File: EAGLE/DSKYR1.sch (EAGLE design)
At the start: 6 parts, among them IC1 74HC595N, IC2 74HC595N, IC3 74HC595N

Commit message: Update guide, finalize gerber files
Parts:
- SV1: device con-lstb:MA05-1 -> con-lsta:FE06-1
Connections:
- removed net N$5: IC1A.SCL, IC2A.SCL, IC3A.SCL, SV1.3
- new net GND: SV1.1
- new net VCC: IC1A.SCL, IC2A.SCL, IC3A.SCL, SV1.4
- net N$1: now also SV1.6; no longer SV1.5
- net N$4: now also SV1.5; no longer SV1.4
- net N$6: now also SV1.2; no longer SV1.1
- net N$8: now also SV1.3; no longer SV1.2
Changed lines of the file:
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@@
 <part name="IC2" library="74xx-eu" library_urn="urn:adsk.eagle:library:85" deviceset="74*595" device="N" package3d_urn="urn:adsk.eagle:package:922/2" technology="HC"/>
 <part name="IC3" library="74xx-eu" library_urn="urn:adsk.eagle:library:85" deviceset="74*595" device="N" package3d_urn="urn:adsk.eagle:package:922/2" technology="HC"/>
-<part name="SV1" library="con-lstb" library_urn="urn:adsk.eagle:library:162" deviceset="MA05-1" device="" package3d_urn="urn:adsk.eagle:package:8332/1"/>
 <part name="D1" library="special" library_urn="urn:adsk.eagle:library:367" deviceset="7SEG-CK" device="" package3d_urn="urn:adsk.eagle:package:26668/2"/>
 <part name="DIS1" library="display-nfd" deviceset="NFD-5641AS-ALT" device=""/>
+<part name="P+1" library="supply1" library_urn="urn:adsk.eagle:library:371" deviceset="VCC" device=""/>
+<part name="SV1" library="con-lsta" library_urn="urn:adsk.eagle:library:161" deviceset="FE06-1" device="" package3d_urn="urn:adsk.eagle:package:8191/1"/>
+<part name="GND1" library="supply1" library_urn="urn:adsk.eagle:library:371" deviceset="GND" device=""/>
 </parts>
 <sheets>
@@
 <attribute name="VALUE" x="88.9" y="15.24" size="1.778" layer="96"/>
 </instance>
-<instance part="SV1" gate="G$1" x="-30.48" y="-35.56" smashed="yes">
-<attribute name="VALUE" x="-31.75" y="-45.72" size="1.778" layer="96"/>
-<attribute name="NAME" x="-31.75" y="-27.178" size="1.778" layer="95"/>
-</instance>
 <instance part="D1" gate="G$1" x="91.44" y="-76.2" smashed="yes">
 <attribute name="NAME" x="86.36" y="-67.945" size="1.778" layer="95"/>
@@
 <attribute name="NAME" x="30.353" y="-81.28" size="1.778" layer="95" rot="R90"/>
 <attribute name="VALUE" x="62.738" y="-81.28" size="1.778" layer="96" rot="R90"/>
+</instance>
+<instance part="P+1" gate="VCC" x="-30.48" y="35.56" smashed="yes" rot="R90">
+<attribute name="VALUE" x="-27.94" y="33.02" size="1.778" layer="96" rot="R180"/>
+</instance>
+<instance part="SV1" gate="G$1" x="-30.48" y="-38.1" smashed="yes">
+<attribute name="VALUE" x="-31.75" y="-48.26" size="1.778" layer="96"/>
+<attribute name="NAME" x="-31.75" y="-27.178" size="1.778" layer="95"/>
+</instance>
+<instance part="GND1" gate="1" x="-12.7" y="-43.18" smashed="yes" rot="R90">
+<attribute name="VALUE" x="-10.16" y="-45.72" size="1.778" layer="96" rot="R90"/>
 </instance>
 </instances>
@@
 <wire x1="-17.78" y1="15.24" x2="-17.78" y2="-30.48" width="0.1524" layer="91"/>
 <wire x1="-17.78" y1="-30.48" x2="-22.86" y2="-30.48" width="0.1524" layer="91"/>
-<pinref part="SV1" gate="G$1" pin="5"/>
+<pinref part="IC2" gate="A" pin="RCK"/>
 <wire x1="-22.86" y1="-30.48" x2="-25.4" y2="-30.48" width="0.1524" layer="91"/>
-<junction x="-22.86" y="-30.48"/>
-<pinref part="IC2" gate="A" pin="RCK"/>
 <wire x1="43.18" y1="30.48" x2="40.64" y2="30.48" width="0.1524" layer="91"/>
 <wire x1="40.64" y1="30.48" x2="40.64" y2="15.24" width="0.1524" layer="91"/>
@@
 <junction x="43.18" y="30.48"/>
 <junction x="83.82" y="30.48"/>
+<pinref part="SV1" gate="G$1" pin="6"/>
+<junction x="-22.86" y="-30.48"/>
 </segment>
 </net>
@@
 <wire x1="5.08" y1="20.32" x2="-15.24" y2="20.32" width="0.1524" layer="91"/>
 <wire x1="-15.24" y1="20.32" x2="-15.24" y2="10.16" width="0.1524" layer="91"/>
-<pinref part="SV1" gate="G$1" pin="4"/>
 <wire x1="-15.24" y1="10.16" x2="-15.24" y2="-33.02" width="0.1524" layer="91"/>
 <wire x1="-15.24" y1="-33.02" x2="-22.86" y2="-33.02" width="0.1524" layer="91"/>
@@
 <wire x1="83.82" y1="10.16" x2="43.18" y2="10.16" width="0.1524" layer="91"/>
 <junction x="43.18" y="10.16"/>
-<junction x="-22.86" y="-33.02"/>
 <junction x="5.08" y="20.32"/>
 <junction x="43.18" y="20.32"/>
 <junction x="83.82" y="20.32"/>
-</segment>
-</net>
-<net name="N$5" class="0">
-<segment>
-<pinref part="IC1" gate="A" pin="SCL"/>
-<wire x1="5.08" y1="35.56" x2="2.54" y2="35.56" width="0.1524" layer="91"/>
-<wire x1="2.54" y1="35.56" x2="-12.7" y2="35.56" width="0.1524" layer="91"/>
-<wire x1="-12.7" y1="35.56" x2="-12.7" y2="-35.56" width="0.1524" layer="91"/>
-<pinref part="SV1" gate="G$1" pin="3"/>
-<wire x1="-12.7" y1="-35.56" x2="-22.86" y2="-35.56" width="0.1524" layer="91"/>
-<pinref part="IC2" gate="A" pin="SCL"/>
-<wire x1="43.18" y1="35.56" x2="40.64" y2="35.56" width="0.1524" layer="91"/>
-<wire x1="40.64" y1="35.56" x2="40.64" y2="50.8" width="0.1524" layer="91"/>
-<wire x1="40.64" y1="50.8" x2="2.54" y2="50.8" width="0.1524" layer="91"/>
-<wire x1="2.54" y1="50.8" x2="2.54" y2="35.56" width="0.1524" layer="91"/>
-<junction x="2.54" y="35.56"/>
-<pinref part="IC3" gate="A" pin="SCL"/>
-<wire x1="83.82" y1="35.56" x2="81.28" y2="35.56" width="0.1524" layer="91"/>
-<wire x1="81.28" y1="35.56" x2="81.28" y2="50.8" width="0.1524" layer="91"/>
-<wire x1="81.28" y1="50.8" x2="40.64" y2="50.8" width="0.1524" layer="91"/>
-<junction x="40.64" y="50.8"/>
-<junction x="-22.86" y="-35.56"/>
-<junction x="5.08" y="35.56"/>
-<junction x="43.18" y="35.56"/>
-<junction x="83.82" y="35.56"/>
+<pinref part="SV1" gate="G$1" pin="5"/>
+<junction x="-22.86" y="-33.02"/>
 </segment>
 </net>
@@
 <wire x1="5.08" y1="38.1" x2="-10.16" y2="38.1" width="0.1524" layer="91"/>
 <wire x1="-10.16" y1="38.1" x2="-10.16" y2="-20.32" width="0.1524" layer="91"/>
-<pinref part="SV1" gate="G$1" pin="2"/>
 <wire x1="-10.16" y1="-20.32" x2="-10.16" y2="-25.4" width="0.1524" layer="91"/>
 <wire x1="-10.16" y1="-25.4" x2="-10.16" y2="-38.1" width="0.1524" layer="91"/>
@@
 <wire x1="78.74" y1="-25.4" x2="-10.16" y2="-25.4" width="0.1524" layer="91"/>
 <junction x="-10.16" y="-25.4"/>
-<junction x="-22.86" y="-38.1"/>
 <junction x="5.08" y="38.1"/>
 <junction x="43.18" y="38.1"/>
 <junction x="83.82" y="38.1"/>
+<pinref part="SV1" gate="G$1" pin="3"/>
+<junction x="-22.86" y="-38.1"/>
 </segment>
 </net>
@@
 <wire x1="5.08" y1="43.18" x2="-7.62" y2="43.18" width="0.1524" layer="91"/>
 <wire x1="-7.62" y1="43.18" x2="-7.62" y2="-40.64" width="0.1524" layer="91"/>
-<pinref part="SV1" gate="G$1" pin="1"/>
 <wire x1="-7.62" y1="-40.64" x2="-22.86" y2="-40.64" width="0.1524" layer="91"/>
+<junction x="5.08" y="43.18"/>
+<pinref part="SV1" gate="G$1" pin="2"/>
 <junction x="-22.86" y="-40.64"/>
-<junction x="5.08" y="43.18"/>
 </segment>
 </net>
@@
 </segment>
 </net>
+<net name="VCC" class="0">
+<segment>
+<pinref part="IC1" gate="A" pin="SCL"/>
+<wire x1="5.08" y1="35.56" x2="2.54" y2="35.56" width="0.1524" layer="91"/>
+<wire x1="2.54" y1="35.56" x2="-12.7" y2="35.56" width="0.1524" layer="91"/>
+<wire x1="-12.7" y1="35.56" x2="-12.7" y2="-35.56" width="0.1524" layer="91"/>
+<wire x1="-12.7" y1="-35.56" x2="-22.86" y2="-35.56" width="0.1524" layer="91"/>
+<pinref part="IC2" gate="A" pin="SCL"/>
+<wire x1="43.18" y1="35.56" x2="40.64" y2="35.56" width="0.1524" layer="91"/>
+<wire x1="40.64" y1="35.56" x2="40.64" y2="50.8" width="0.1524" layer="91"/>
+<wire x1="40.64" y1="50.8" x2="2.54" y2="50.8" width="0.1524" layer="91"/>
+<wire x1="2.54" y1="50.8" x2="2.54" y2="35.56" width="0.1524" layer="91"/>
+<junction x="2.54" y="35.56"/>
+<pinref part="IC3" gate="A" pin="SCL"/>
+<wire x1="83.82" y1="35.56" x2="81.28" y2="35.56" width="0.1524" layer="91"/>
+<wire x1="81.28" y1="35.56" x2="81.28" y2="50.8" width="0.1524" layer="91"/>
+<wire x1="81.28" y1="50.8" x2="40.64" y2="50.8" width="0.1524" layer="91"/>
+<junction x="40.64" y="50.8"/>
+<junction x="5.08" y="35.56"/>
+<junction x="43.18" y="35.56"/>
+<junction x="83.82" y="35.56"/>
+<pinref part="P+1" gate="VCC" pin="VCC"/>
+<wire x1="-27.94" y1="35.56" x2="-12.7" y2="35.56" width="0.1524" layer="91"/>
+<junction x="-12.7" y="35.56"/>
+<pinref part="SV1" gate="G$1" pin="4"/>
+<junction x="-22.86" y="-35.56"/>
+</segment>
+</net>
+<net name="GND" class="0">
+<segment>
+<pinref part="GND1" gate="1" pin="GND"/>
+<pinref part="SV1" gate="G$1" pin="1"/>
+<wire x1="-15.24" y1="-43.18" x2="-22.86" y2="-43.18" width="0.1524" layer="91"/>
+<junction x="-22.86" y="-43.18"/>
+</segment>
+</net>

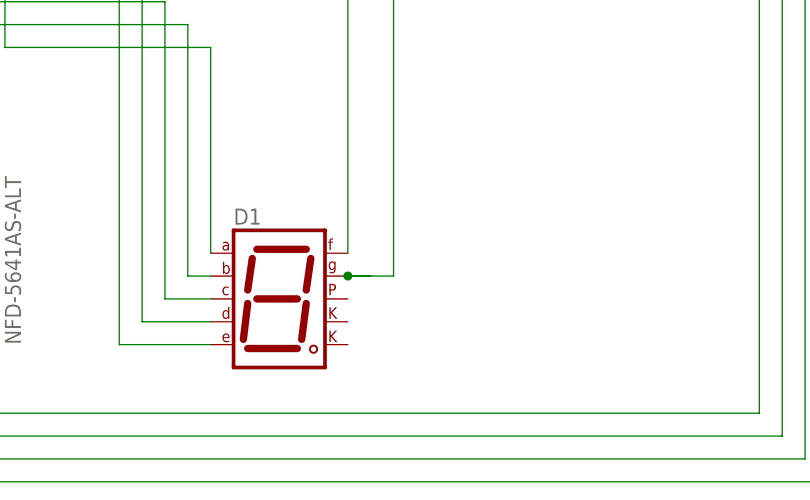
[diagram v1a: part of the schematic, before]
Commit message: Connect ground lines of R1D5
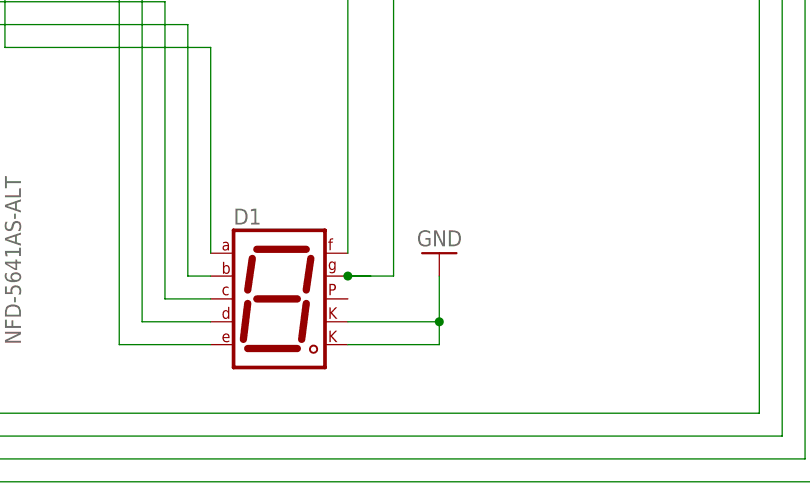
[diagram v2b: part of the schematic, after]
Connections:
- net GND: now also D1.CK1, D1.CK2
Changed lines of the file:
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@@
 <part name="SV1" library="con-lsta" library_urn="urn:adsk.eagle:library:161" deviceset="FE06-1" device="" package3d_urn="urn:adsk.eagle:package:8191/1"/>
 <part name="GND1" library="supply1" library_urn="urn:adsk.eagle:library:371" deviceset="GND" device=""/>
+<part name="GND2" library="supply1" library_urn="urn:adsk.eagle:library:371" deviceset="GND" device=""/>
 </parts>
 <sheets>
@@
 <instance part="GND1" gate="1" x="-12.7" y="-43.18" smashed="yes" rot="R90">
 <attribute name="VALUE" x="-10.16" y="-45.72" size="1.778" layer="96" rot="R90"/>
+</instance>
+<instance part="GND2" gate="1" x="109.22" y="-71.12" smashed="yes" rot="R180">
+<attribute name="VALUE" x="111.76" y="-68.58" size="1.778" layer="96" rot="R180"/>
 </instance>
 </instances>
@@
 <junction x="-22.86" y="-43.18"/>
 </segment>
-</net>
+<segment>
+<pinref part="D1" gate="G$1" pin="CK1"/>
+<wire x1="99.06" y1="-78.74" x2="109.22" y2="-78.74" width="0.1524" layer="91"/>
+<pinref part="D1" gate="G$1" pin="CK2"/>
+<wire x1="99.06" y1="-81.28" x2="109.22" y2="-81.28" width="0.1524" layer="91"/>
+<wire x1="109.22" y1="-81.28" x2="109.22" y2="-78.74" width="0.1524" layer="91"/>
+<junction x="109.22" y="-78.74"/>
+<wire x1="109.22" y1="-78.74" x2="109.22" y2="-73.66" width="0.1524" layer="91"/>
+<pinref part="GND2" gate="1" pin="GND"/>
+</segment>
+</net>
